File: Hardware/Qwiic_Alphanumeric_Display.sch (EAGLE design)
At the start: 34 parts, among them J4 Vertical Qwiic Connector, J5 Vertical Qwiic Connector, U1 Alphanumeric Display, U2 XC9140

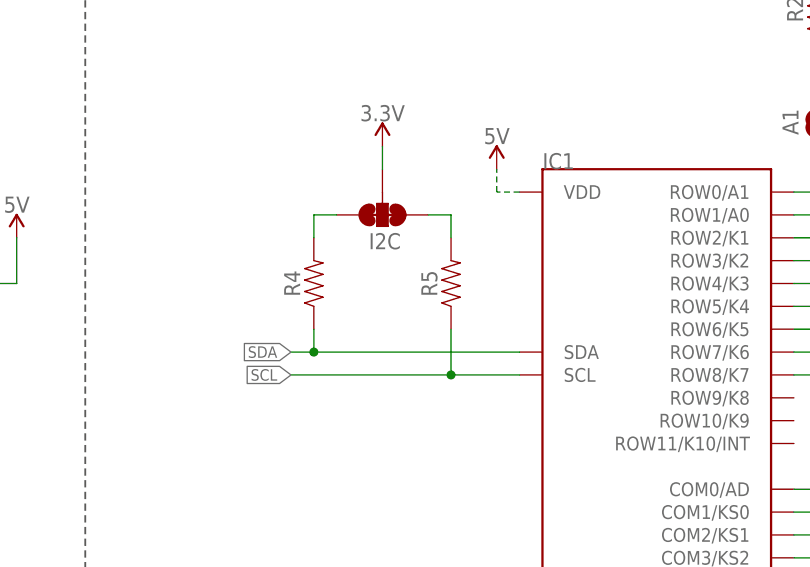
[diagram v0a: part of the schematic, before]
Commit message: Change pullups from 1k to 4.7k
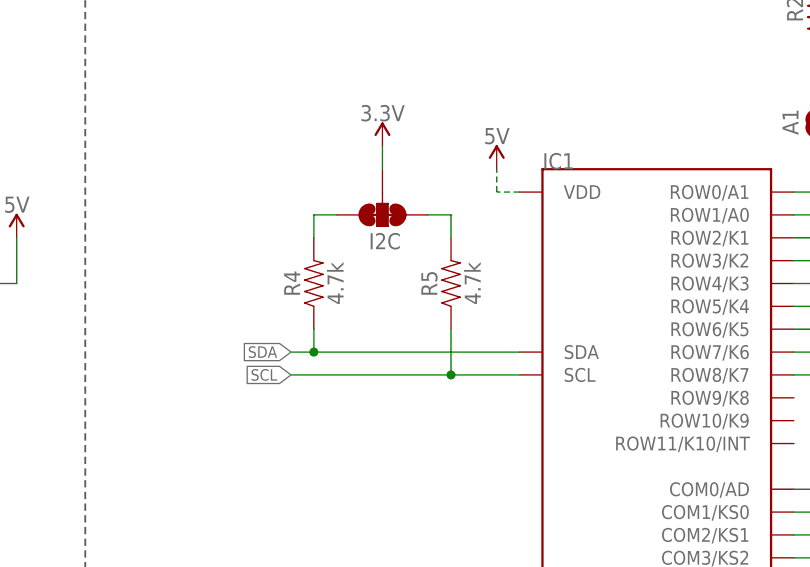
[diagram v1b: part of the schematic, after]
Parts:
- R4, R5: value 1KOHM-0402-1/16W-1% -> 4.7k; device SparkFun-Resistors:1KOHM-0402-1/16W-1% -> SparkFun-Resistors:4.7KOHM-0402T-1/16W-1%
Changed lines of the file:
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@@
 <grid distance="0.1" unitdist="inch" unit="inch" style="lines" multiple="1" display="no" altdistance="0.01" altunitdist="inch" altunit="inch"/>
 <layers>
-<layer number="1" name="Top" color="4" fill="1" visible="yes" active="no"/>
-<layer number="2" name="Route2" color="16" fill="1" visible="yes" active="no"/>
-<layer number="15" name="Route15" color="23" fill="1" visible="yes" active="no"/>
-<layer number="16" name="Bottom" color="1" fill="1" visible="yes" active="no"/>
-<layer number="17" name="Pads" color="2" fill="1" visible="yes" active="no"/>
-<layer number="18" name="Vias" color="2" fill="1" visible="yes" active="no"/>
-<layer number="19" name="Unrouted" color="6" fill="1" visible="yes" active="no"/>
-<layer number="20" name="Dimension" color="24" fill="1" visible="yes" active="no"/>
-<layer number="21" name="tPlace" color="16" fill="1" visible="yes" active="no"/>
-<layer number="22" name="bPlace" color="14" fill="1" visible="yes" active="no"/>
-<layer number="23" name="tOrigins" color="15" fill="1" visible="yes" active="no"/>
-<layer number="24" name="bOrigins" color="15" fill="1" visible="yes" active="no"/>
-<layer number="25" name="tNames" color="7" fill="1" visible="yes" active="no"/>
-<layer number="26" name="bNames" color="7" fill="1" visible="yes" active="no"/>
-<layer number="27" name="tValues" color="7" fill="1" visible="yes" active="no"/>
-<layer number="28" name="bValues" color="7" fill="1" visible="yes" active="no"/>
+<layer number="1" name="Top" color="4" fill="1" visible="no" active="no"/>
+<layer number="2" name="Route2" color="16" fill="1" visible="no" active="no"/>
+<layer number="15" name="Route15" color="23" fill="1" visible="no" active="no"/>
+<layer number="16" name="Bottom" color="1" fill="1" visible="no" active="no"/>
+<layer number="17" name="Pads" color="2" fill="1" visible="no" active="no"/>
+<layer number="18" name="Vias" color="2" fill="1" visible="no" active="no"/>
+<layer number="19" name="Unrouted" color="6" fill="1" visible="no" active="no"/>
+<layer number="20" name="Dimension" color="24" fill="1" visible="no" active="no"/>
+<layer number="21" name="tPlace" color="16" fill="1" visible="no" active="no"/>
+<layer number="22" name="bPlace" color="14" fill="1" visible="no" active="no"/>
+<layer number="23" name="tOrigins" color="15" fill="1" visible="no" active="no"/>
+<layer number="24" name="bOrigins" color="15" fill="1" visible="no" active="no"/>
+<layer number="25" name="tNames" color="7" fill="1" visible="no" active="no"/>
+<layer number="26" name="bNames" color="7" fill="1" visible="no" active="no"/>
+<layer number="27" name="tValues" color="7" fill="1" visible="no" active="no"/>
+<layer number="28" name="bValues" color="7" fill="1" visible="no" active="no"/>
 <layer number="29" name="tStop" color="7" fill="3" visible="no" active="no"/>
 <layer number="30" name="bStop" color="7" fill="6" visible="no" active="no"/>
@@
 <layer number="35" name="tGlue" color="7" fill="4" visible="no" active="no"/>
 <layer number="36" name="bGlue" color="7" fill="5" visible="no" active="no"/>
-<layer number="37" name="tTest" color="7" fill="1" visible="yes" active="no"/>
-<layer number="38" name="bTest" color="7" fill="1" visible="yes" active="no"/>
+<layer number="37" name="tTest" color="7" fill="1" visible="no" active="no"/>
+<layer number="38" name="bTest" color="7" fill="1" visible="no" active="no"/>
 <layer number="39" name="tKeepout" color="4" fill="11" visible="no" active="no"/>
 <layer number="40" name="bKeepout" color="1" fill="11" visible="no" active="no"/>
@@
 <layer number="44" name="Drills" color="7" fill="1" visible="no" active="no"/>
 <layer number="45" name="Holes" color="7" fill="1" visible="no" active="no"/>
-<layer number="46" name="Milling" color="3" fill="1" visible="yes" active="no"/>
-<layer number="47" name="Measures" color="7" fill="1" visible="yes" active="no"/>
-<layer number="48" name="Document" color="7" fill="1" visible="yes" active="no"/>
-<layer number="49" name="Reference" color="7" fill="1" visible="yes" active="no"/>
-<layer number="50" name="dxf" color="7" fill="1" visible="yes" active="no"/>
-<layer number="51" name="tDocu" color="6" fill="1" visible="yes" active="no"/>
-<layer number="52" name="bDocu" color="7" fill="1" visible="yes" active="no"/>
-<layer number="53" name="tGND_GNDA" color="7" fill="9" visible="yes" active="no"/>
-<layer number="54" name="bGND_GNDA" color="1" fill="9" visible="yes" active="no"/>
-<layer number="56" name="wert" color="7" fill="1" visible="yes" active="no"/>
-<layer number="57" name="tCAD" color="7" fill="1" visible="yes" active="no"/>
-<layer number="58" name="bCAD" color="7" fill="1" visible="yes" active="no"/>
-<layer number="59" name="tCarbon" color="7" fill="1" visible="yes" active="no"/>
-<layer number="60" name="bCarbon" color="7" fill="1" visible="yes" active="no"/>
+<layer number="46" name="Milling" color="3" fill="1" visible="no" active="no"/>
+<layer number="47" name="Measures" color="7" fill="1" visible="no" active="no"/>
+<layer number="48" name="Document" color="7" fill="1" visible="no" active="no"/>
+<layer number="49" name="Reference" color="7" fill="1" visible="no" active="no"/>
+<layer number="50" name="dxf" color="7" fill="1" visible="no" active="no"/>
+<layer number="51" name="tDocu" color="6" fill="1" visible="no" active="no"/>
+<layer number="52" name="bDocu" color="7" fill="1" visible="no" active="no"/>
+<layer number="53" name="tGND_GNDA" color="7" fill="9" visible="no" active="no"/>
+<layer number="54" name="bGND_GNDA" color="1" fill="9" visible="no" active="no"/>
+<layer number="56" name="wert" color="7" fill="1" visible="no" active="no"/>
+<layer number="57" name="tCAD" color="7" fill="1" visible="no" active="no"/>
+<layer number="58" name="bCAD" color="7" fill="1" visible="no" active="no"/>
+<layer number="59" name="tCarbon" color="7" fill="1" visible="no" active="no"/>
+<layer number="60" name="bCarbon" color="7" fill="1" visible="no" active="no"/>
 <layer number="88" name="SimResults" color="9" fill="1" visible="yes" active="yes"/>
 <layer number="89" name="SimProbes" color="9" fill="1" visible="yes" active="yes"/>
@@
 <part name="LOGO1" library="SparkFun-Aesthetics" deviceset="OSHW-LOGO" device="MINI"/>
 <part name="GND6" library="SparkFun-PowerSymbols" deviceset="GND" device=""/>
-<part name="R4" library="SparkFun-Resistors" deviceset="1KOHM" device="-0402-1/16W-1%" value="1KOHM-0402-1/16W-1%"/>
-<part name="R5" library="SparkFun-Resistors" deviceset="1KOHM" device="-0402-1/16W-1%" value="1KOHM-0402-1/16W-1%"/>
+<part name="R4" library="SparkFun-Resistors" deviceset="4.7KOHM" device="-0402T-1/16W-1%" value="4.7k"/>
+<part name="R5" library="SparkFun-Resistors" deviceset="4.7KOHM" device="-0402T-1/16W-1%" value="4.7k"/>
 <part name="A1" library="SparkFun-Jumpers" deviceset="JUMPER-SMT_2_NO" device="_SILK" package3d_urn="urn:adsk.eagle:package:39279/1"/>
 <part name="A0" library="SparkFun-Jumpers" deviceset="JUMPER-SMT_2_NO" device="_SILK" package3d_urn="urn:adsk.eagle:package:39279/1"/>
@@
 <instance part="R4" gate="G$1" x="83.82" y="142.24" smashed="yes" rot="R90">
 <attribute name="NAME" x="82.296" y="142.24" size="1.778" layer="95" font="vector" rot="R90" align="bottom-center"/>
+<attribute name="VALUE" x="85.344" y="142.24" size="1.778" layer="96" font="vector" rot="R90" align="top-center"/>
 </instance>
 <instance part="R5" gate="G$1" x="99.06" y="142.24" smashed="yes" rot="R90">
 <attribute name="NAME" x="97.536" y="142.24" size="1.778" layer="95" font="vector" rot="R90" align="bottom-center"/>
+<attribute name="VALUE" x="100.584" y="142.24" size="1.778" layer="96" font="vector" rot="R90" align="top-center"/>
 </instance>
 <instance part="A1" gate="G$1" x="139.7" y="160.02" smashed="yes" rot="R90">
